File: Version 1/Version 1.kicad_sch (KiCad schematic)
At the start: 73 parts, among them J1 Conn_01x05, Q1 IPP015N04NF2SAKMA1, Q2 IPP015N04NF2SAKMA1, Q3 IPP015N04NF2SAKMA1, Q4 IPP015N04NF2SAKMA1, Q5 IPP015N04NF2SAKMA1, Q6 IPP015N04NF2SAKMA1, U1 TPS62932, U2 TPS62932, U3 TPS62932, U4 IRS2004, U5 IRS2004, U6 IRS2004, U7 YAAJ_BlackPill_SWD_BreakoutV2

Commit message: updated circuit
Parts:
- added J_RPI1: Conn_01x04, Connector_JST:JST_ACH_BM04B-ACHSS-A-GAN-ETF_1x04-1MP_P1.20mm_Vertical, symbol Connector_Generic:Conn_01x04
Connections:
- net INH_U is gone; now on net IN_U: R5.1, U4.2 (IN)
- net INH_V is gone; now on net IN_V: R6.1, U5.2 (IN)
- net INH_W is gone; now on net IN_W: R8.1, U6.2 (IN)
- net +5V: now also J_RPI1.1 (Pin_1)
- net GND: now also J_RPI1.4 (Pin_4)
- net HallU: now also U7.33 (B5); no longer U7.2 (C13)
- net HallV: now also U7.34 (B6); no longer U7.3 (C14)
- net HallW: now also U7.35 (B7); no longer U7.4 (C15)
- net IN_U: now reaches U7.12 (A6)
- net IN_V: now reaches U7.13 (A7)
- net IN_W: now reaches U7.14 (B0)
- net SCL_RPI: now reaches U7.17 (B10)
- net SCL_RPI: now also J_RPI1.2 (Pin_2)
- net SDA_RPI: now reaches U7.31 (B3)
- net SDA_RPI: now also J_RPI1.3 (Pin_3)
- net INL_U renamed SD_U
- net SD_U: now also U7.2 (C13)
- net INL_V renamed SD_V
- net SD_V: now also U7.3 (C14)
- net INL_W renamed SD_W
- net SD_W: now also U7.4 (C15)
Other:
- note added: "Main circuit power connector"
- note added: "RPI Connector"
- note removed: "Connector"
- moved on the sheet: D1, Jin1, Jout1, U7

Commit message: latest 3d components
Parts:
- U4, U5, U6: footprint (none) -> IRS2004PBF:DIP762W56P254L988H533Q8N
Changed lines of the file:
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@@
 			)
 		)
-		(property "Footprint" ""
+		(property "Footprint" "IRS2004PBF:DIP762W56P254L988H533Q8N"
 			(at 189.23 104.14 0)
 			(effects
@@
 			)
 		)
-		(property "Footprint" ""
+		(property "Footprint" "IRS2004PBF:DIP762W56P254L988H533Q8N"
 			(at 148.59 104.14 0)
 			(effects
@@
 			)
 		)
-		(property "Footprint" ""
+		(property "Footprint" "IRS2004PBF:DIP762W56P254L988H533Q8N"
 			(at 229.87 104.14 0)
 			(effects

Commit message: udpated pcb
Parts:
- added U8, V1, W1: Conn_01x01_Socket, MountingHole:MountingHole_4.3mm_M4_DIN965_Pad, symbol Connector:Conn_01x01_Socket
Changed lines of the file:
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@@
 	)
 	(symbol
+		(lib_id "Connector:Conn_01x01_Socket")
+		(at 337.82 142.24 0)
+		(unit 1)
+		(exclude_from_sim no)
+		(in_bom yes)
+		(on_board yes)
+		(dnp no)
+		(fields_autoplaced yes)
+		(property "Reference" "W1"
+			(at 339.09 140.9699 0)
+			(effects
+				(font
+					(size 1.27 1.27)
+				)
+				(justify left)
+			)
+		)
+		(property "Value" "Conn_01x01_Socket"
+			(at 339.09 143.5099 0)
+			(effects
+				(font
+					(size 1.27 1.27)
+				)
+				(justify left)
+			)
+		)
+		(property "Footprint" "MountingHole:MountingHole_4.3mm_M4_DIN965_Pad"
+			(at 337.82 142.24 0)
+			(effects
+				(font
+					(size 1.27 1.27)
+				)
+				(hide yes)
+			)
+		)
+		(property "Datasheet" "~"
+			(at 337.82 142.24 0)
+			(effects
+				(font
+					(size 1.27 1.27)
+				)
+				(hide yes)
+			)
+		)
+		(property "Description" "Generic connector, single row, 01x01, script generated"
+			(at 337.82 142.24 0)
+			(effects
+				(font
+					(size 1.27 1.27)
+				)
+				(hide yes)
+			)
+		)
+		(pin "1"
+		)
+		(instances
+			(project "Version 1"
+				(path "/1b67c1a2-c765-4a1d-8ccd-1a2054fe1222"
+					(reference "W1")
+					(unit 1)
+				)
+			)
+		)
+	)
+	(symbol
 		(lib_id "Device:C")
 		(at 43.18 35.56 90)
@@
 	)
 	(symbol
+		(lib_id "Connector:Conn_01x01_Socket")
+		(at 337.82 137.16 0)
+		(unit 1)
+		(exclude_from_sim no)
+		(in_bom yes)
+		(on_board yes)
+		(dnp no)
+		(fields_autoplaced yes)
+		(property "Reference" "V1"
+			(at 339.09 135.8899 0)
+			(effects
+				(font
+					(size 1.27 1.27)
+				)
+				(justify left)
+			)
+		)
+		(property "Value" "Conn_01x01_Socket"
+			(at 339.09 138.4299 0)
+			(effects
+				(font
+					(size 1.27 1.27)
+				)
+				(justify left)
+			)
+		)
+		(property "Footprint" "MountingHole:MountingHole_4.3mm_M4_DIN965_Pad"
+			(at 337.82 137.16 0)
+			(effects
+				(font
+					(size 1.27 1.27)
+				)
+				(hide yes)
+			)
+		)
+		(property "Datasheet" "~"
+			(at 337.82 137.16 0)
+			(effects
+				(font
+					(size 1.27 1.27)
+				)
+				(hide yes)
+			)
+		)
+		(property "Description" "Generic connector, single row, 01x01, script generated"
+			(at 337.82 137.16 0)
+			(effects
+				(font
+					(size 1.27 1.27)
+				)
+				(hide yes)
+			)
+		)
+		(pin "1"
+		)
+		(instances
+			(project "Version 1"
+				(path "/1b67c1a2-c765-4a1d-8ccd-1a2054fe1222"
+					(reference "V1")
+					(unit 1)
+				)
+			)
+		)
+	)
+	(symbol
 		(lib_id "Device:D")
 		(at 327.66 93.98 180)
@@
 					(unit 1)
 				)
+			)
+		)
+	)
+	(symbol
+		(lib_id "Connector:Conn_01x01_Socket")
+		(at 337.82 132.08 0)
+		(unit 1)
+		(exclude_from_sim no)
+		(in_bom yes)
+		(on_board yes)
+		(dnp no)
+		(fields_autoplaced yes)
+		(property "Reference" "U8"
+			(at 339.09 130.8099 0)
+			(effects
+				(font
+					(size 1.27 1.27)
+				)
+				(justify left)
+			)
+		)
+		(property "Value" "Conn_01x01_Socket"
+			(at 339.09 133.3499 0)
+			(effects
+				(font
+					(size 1.27 1.27)
+				)
+				(justify left)
+			)
+		)
+		(property "Footprint" "MountingHole:MountingHole_4.3mm_M4_DIN965_Pad"
+			(at 337.82 132.08 0)
+			(effects
+				(font
+					(size 1.27 1.27)
+				)
+				(hide yes)
+			)
+		)
+		(property "Datasheet" "~"
+			(at 337.82 132.08 0)
+			(effects
+				(font
+					(size 1.27 1.27)
+				)
+				(hide yes)
+			)
+		)
+		(property "Description" "Generic connector, single row, 01x01, script generated"
+			(at 337.82 132.08 0)
+			(effects
+				(font
+					(size 1.27 1.27)
+				)
+				(hide yes)
+			)
+		)
+		(pin "1"
+		)
+		(instances
+			(project "Version 1"
+				(path "/1b67c1a2-c765-4a1d-8ccd-1a2054fe1222"
+					(reference "U8")
+					(unit 1)
+				)

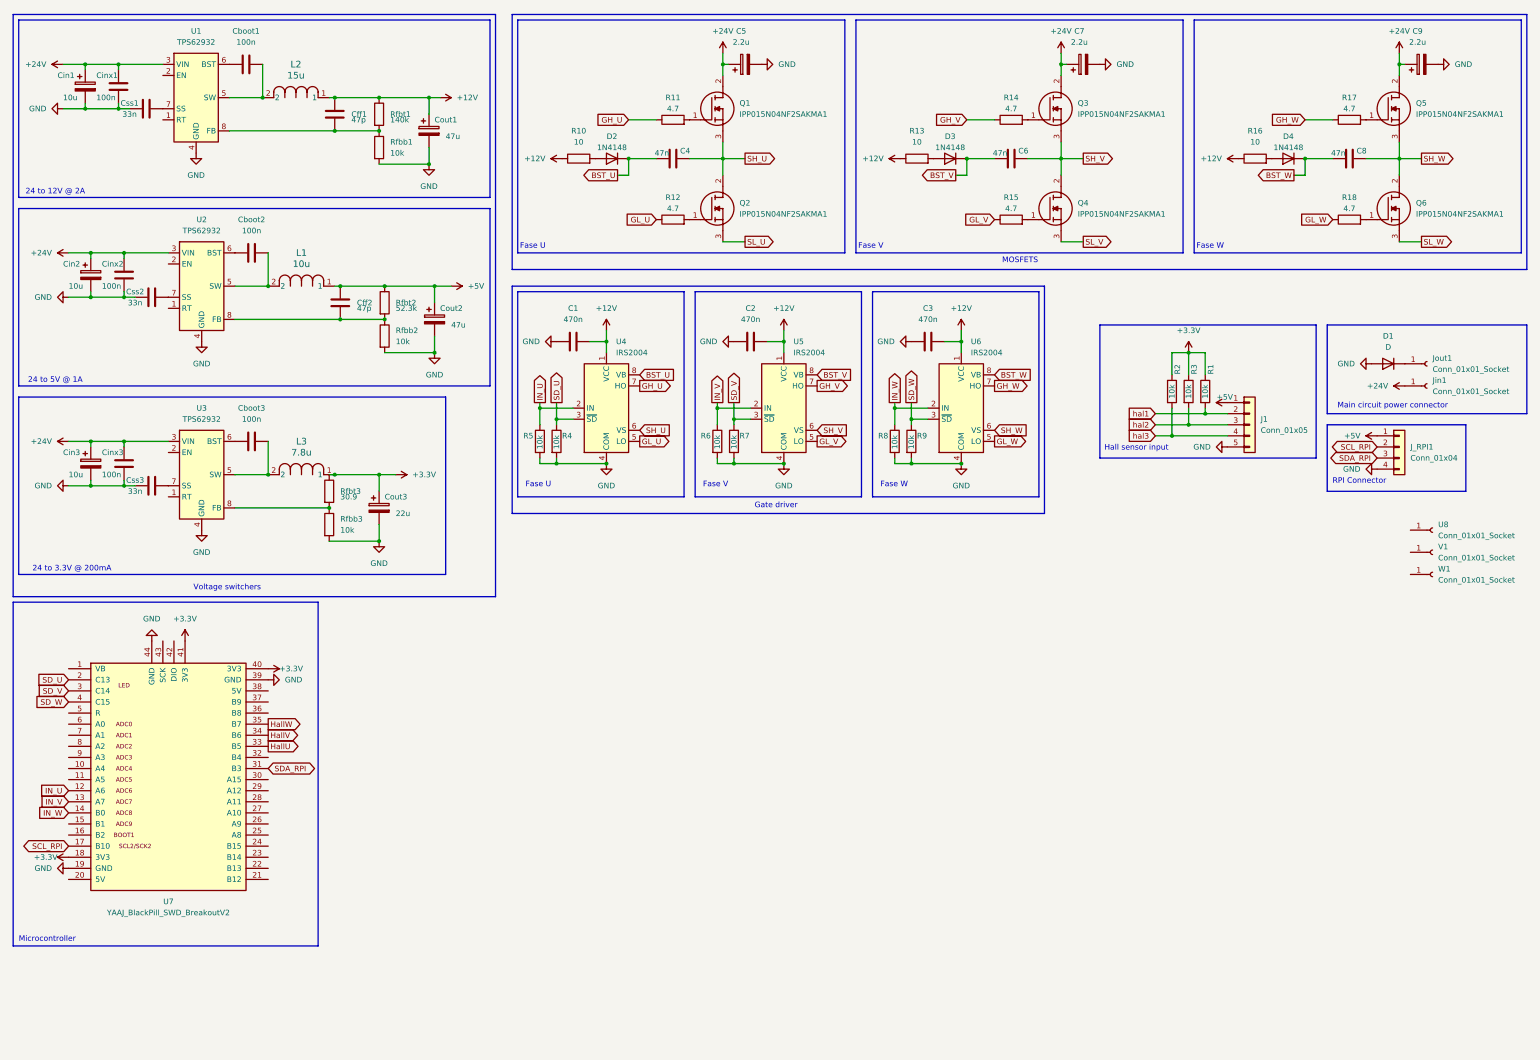
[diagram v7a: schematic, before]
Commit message: Added Connectors SPI and USART
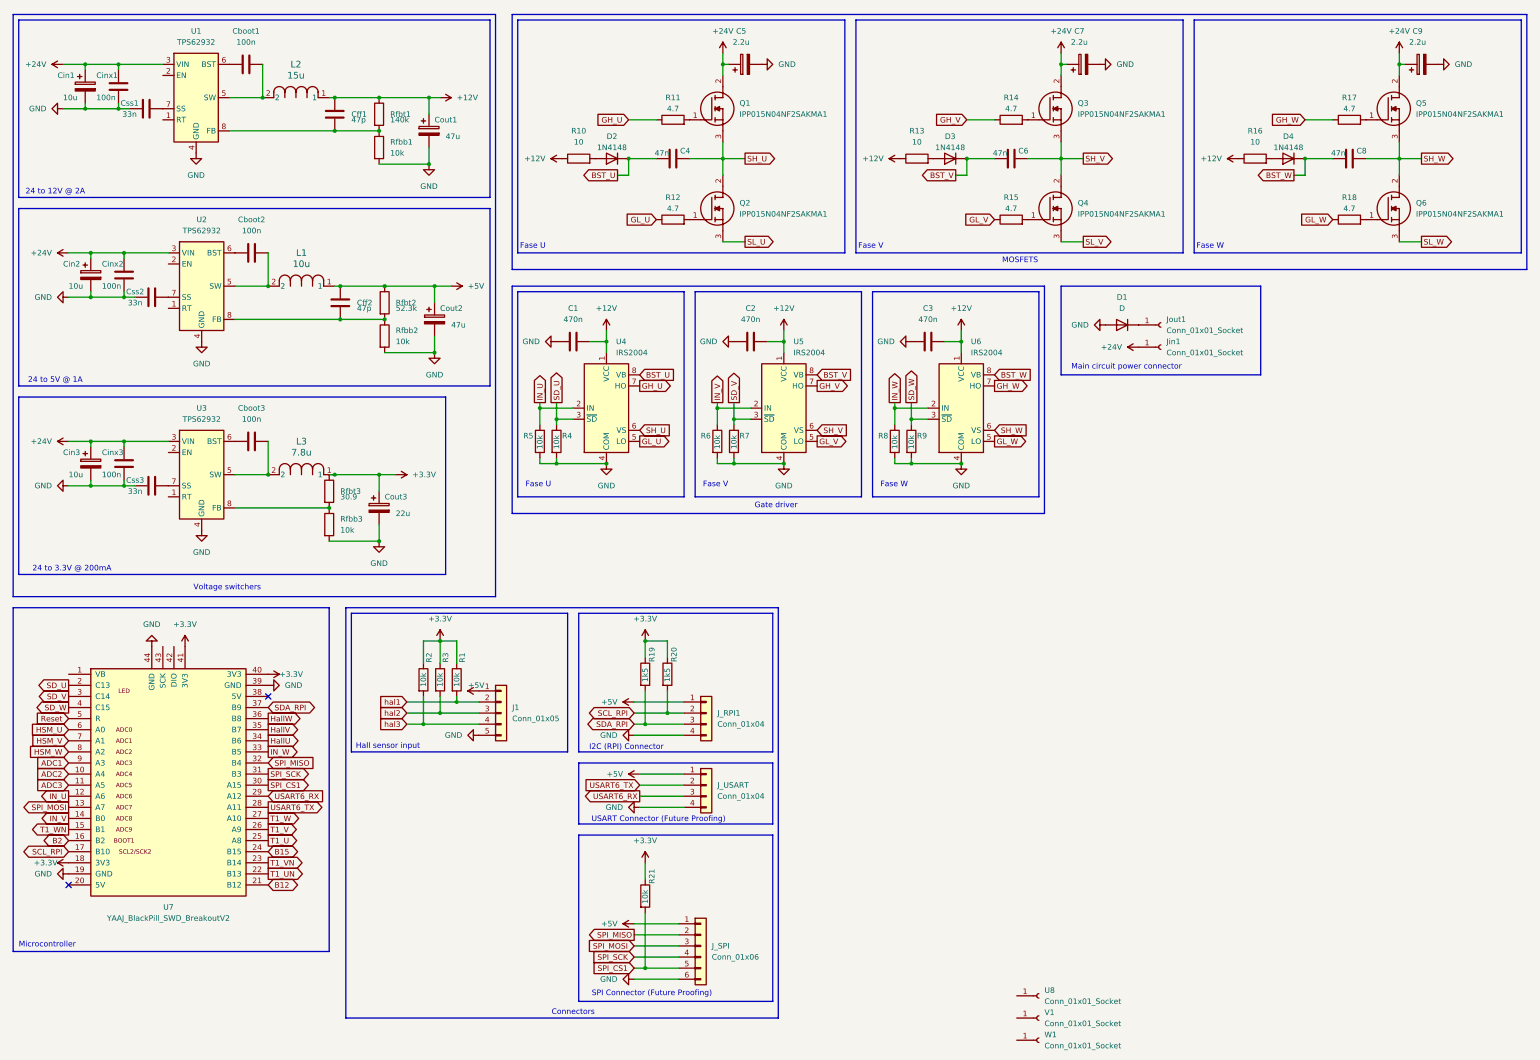
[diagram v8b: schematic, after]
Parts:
- added J_SPI: Conn_01x06, symbol Connector_Generic:Conn_01x06
- added J_USART: Conn_01x04, Connector_JST:JST_ACH_BM04B-ACHSS-A-GAN-ETF_1x04-1MP_P1.20mm_Vertical, symbol Connector_Generic:Conn_01x04
- added R19, R20: 1k5, symbol Device:R
- added R21: 10k, symbol Device:R
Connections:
- net +3.3V: now also R19.1, R20.1, R21.1
- net +5V: now also J_SPI.1 (Pin_1), J_USART.1 (Pin_1)
- net GND: now also J_SPI.6 (Pin_6), J_USART.4 (Pin_4)
- net HallU: now also U7.34 (B6); no longer U7.33 (B5)
- net HallV: now also U7.35 (B7); no longer U7.34 (B6)
- net HallW: now also U7.36 (B8); no longer U7.35 (B7)
- net IN_V: now also U7.14 (B0); no longer U7.13 (A7)
- net IN_W: now also U7.33 (B5); no longer U7.14 (B0)
- net SCL_RPI: now also R20.2
- net SDA_RPI: now also U7.37 (B9), R19.2; no longer U7.31 (B3)
- net ADC2: now reaches U7.10 (A4)
- net ADC3: now reaches U7.11 (A5)
- net T1_WN: now reaches U7.15 (B1)
- net B2: now reaches U7.16 (B2)
- net B12: now reaches U7.21 (B12)
- net T1_UN: now reaches U7.22 (B13)
- net T1_VN: now reaches U7.23 (B14)
- net B15: now reaches U7.24 (B15)
- net T1_U: now reaches U7.25 (A8)
- net T1_V: now reaches U7.26 (A9)
- net T1_W: now reaches U7.27 (A10)
- net USART6_TX: now reaches U7.28 (A11)
- net USART6_TX: now also J_USART.2 (Pin_2)
- net USART6_RX: now reaches U7.29 (A12)
- net USART6_RX: now also J_USART.3 (Pin_3)
- net SPI_CS1: now reaches U7.30 (A15)
- net SPI_CS1: now also J_SPI.5 (Pin_5), R21.2
- net SPI_MISO: now reaches U7.32 (B4)
- net SPI_MISO: now also J_SPI.2 (Pin_2)
- net Reset: now reaches U7.5 (R)
- net HSM_U: now reaches U7.6 (A0)
- net HSM_V: now reaches U7.7 (A1)
- net HSM_W: now reaches U7.8 (A2)
- net ADC1: now reaches U7.9 (A3)
- new net SPI_MOSI: J_SPI.3 (Pin_3), U7.13 (A7)
- new net SPI_SCK: J_SPI.4 (Pin_4), U7.31 (B3)
- no-connect marks 0 -> 2
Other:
- note added: "Connectors"
- note added: "I2C (RPI) Connector"
- note added: "SPI Connector (Future Proofing)"
- note added: "USART Connector (Future Proofing)"
- note removed: "RPI Connector"
- moved on the sheet: D1, J1, J_RPI1, Jin1, Jout1, R1, R2, R3, U7, U8, V1, W1
